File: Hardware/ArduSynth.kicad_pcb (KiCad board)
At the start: 2 copper layers, 71.1 x 45.7 mm, 21 parts, among them J1 STEREO_JACK_3.5MM, J2 STEREO_JACK_3.5MM, P1 ARD_CONN_8, P2 ADR_CONN_6, P3 ARD_CONN_10, P4 ARD_CONN_8, SW1 SW_12X12MM

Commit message: Fixed lables on sch
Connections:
- net N-0000022 renamed /ADJ3
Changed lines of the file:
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@@
     (links 40)
     (no_connects 40)
-    (area 59.400999 86.425309 170.497501 152.806401)
+    (area 93.690999 34.28873 168.560044 81.330001)
     (thickness 1.6)
     (drawings 4)
@@
   (net 1 /ADJ1)
   (net 2 /ADJ2)
-  (net 3 /ADJ4)
-  (net 4 /ADJ5)
-  (net 5 "/AUDIO OUT")
-  (net 6 /CV)
-  (net 7 /TRIGGER)
-  (net 8 N-0000013)
-  (net 9 N-0000018)
-  (net 10 N-0000022)
+  (net 3 /ADJ3)
+  (net 4 /ADJ4)
+  (net 5 /ADJ5)
+  (net 6 "/AUDIO OUT")
+  (net 7 /CV)
+  (net 8 /TRIGGER)
+  (net 9 N-0000014)
+  (net 10 N-0000034)
   (net 11 N-0000035)
   (net 12 N-0000036)
   (net 13 N-0000037)
-  (net 14 N-0000038)
+  (net 14 N-0000039)
   (net 15 VDD)
   (net 16 VSS)
@@
     (add_net /ADJ1)
     (add_net /ADJ2)
+    (add_net /ADJ3)
     (add_net /ADJ4)
     (add_net /ADJ5)
@@
     (add_net /CV)
     (add_net /TRIGGER)
-    (add_net N-0000013)
-    (add_net N-0000018)
-    (add_net N-0000022)
+    (add_net N-0000014)
+    (add_net N-0000034)
     (add_net N-0000035)
     (add_net N-0000036)
     (add_net N-0000037)
-    (add_net N-0000038)
+    (add_net N-0000039)
     (add_net VDD)
     (add_net VSS)
@@
     (pad 1 thru_hole circle (at 3.81 -2.54) (size 1.397 1.397) (drill 0.8128)
       (layers *.Cu *.Mask F.SilkS)
-      (net 7 /TRIGGER)
+      (net 8 /TRIGGER)
     )
     (pad 2 thru_hole circle (at 3.81 2.54) (size 1.397 1.397) (drill 0.8128)
       (layers *.Cu *.Mask F.SilkS)
-      (net 7 /TRIGGER)
+      (net 8 /TRIGGER)
     )
     (pad 1 thru_hole circle (at -3.81 -2.54) (size 1.397 1.397) (drill 0.8128)
       (layers *.Cu *.Mask F.SilkS)
-      (net 7 /TRIGGER)
+      (net 8 /TRIGGER)
     )
     (pad 2 thru_hole circle (at -3.81 2.54) (size 1.397 1.397) (drill 0.8128)
       (layers *.Cu *.Mask F.SilkS)
-      (net 7 /TRIGGER)
+      (net 8 /TRIGGER)
     )
   )
@@
     (pad 1 thru_hole circle (at -5.08 0 180) (size 1.524 1.524) (drill 0.8128)
       (layers *.Cu *.Mask F.SilkS)
-      (net 14 N-0000038)
+      (net 14 N-0000039)
     )
     (pad 2 thru_hole circle (at 5.08 0 180) (size 1.524 1.524) (drill 0.8128)
@@
     (pad 1 thru_hole circle (at -5.08 0) (size 1.524 1.524) (drill 0.8128)
       (layers *.Cu *.Mask F.SilkS)
-      (net 6 /CV)
+      (net 7 /CV)
     )
     (pad 2 thru_hole circle (at 5.08 0) (size 1.524 1.524) (drill 0.8128)
       (layers *.Cu *.Mask F.SilkS)
-      (net 8 N-0000013)
+      (net 9 N-0000014)
     )
     (model discret/resistor.wrl
@@
     (pad 2 thru_hole circle (at 5.08 0 180) (size 1.524 1.524) (drill 0.8128)
       (layers *.Cu *.Mask F.SilkS)
-      (net 14 N-0000038)
+      (net 14 N-0000039)
     )
     (model discret/resistor.wrl
@@
     (pad 1 thru_hole circle (at -1.27 0 180) (size 1.397 1.397) (drill 0.8128)
       (layers *.Cu *.Mask F.SilkS)
-      (net 8 N-0000013)
+      (net 9 N-0000014)
     )
     (pad 2 thru_hole circle (at 1.27 0 180) (size 1.397 1.397) (drill 0.8128)
@@
     (pad 1 thru_hole circle (at -1.27 0) (size 1.397 1.397) (drill 0.8128)
       (layers *.Cu *.Mask F.SilkS)
-      (net 14 N-0000038)
+      (net 14 N-0000039)
     )
     (pad 2 thru_hole circle (at 1.27 0) (size 1.397 1.397) (drill 0.8128)
@@
     (pad 6 thru_hole circle (at 3.81 0) (size 1.397 1.397) (drill 0.8128)
       (layers *.Cu *.Mask F.SilkS)
-      (net 7 /TRIGGER)
+      (net 8 /TRIGGER)
     )
     (pad 7 thru_hole circle (at 6.35 0) (size 1.397 1.397) (drill 0.8128)
@@
     (pad 1 thru_hole rect (at -6.35 0) (size 1.397 1.397) (drill 0.8128)
       (layers *.Cu *.Mask F.SilkS)
-      (net 8 N-0000013)
+      (net 9 N-0000014)
     )
     (pad 2 thru_hole circle (at -3.81 0) (size 1.397 1.397) (drill 0.8128)
       (layers *.Cu *.Mask F.SilkS)
-      (net 4 /ADJ5)
+      (net 5 /ADJ5)
     )
     (pad 3 thru_hole circle (at -1.27 0) (size 1.397 1.397) (drill 0.8128)
       (layers *.Cu *.Mask F.SilkS)
-      (net 3 /ADJ4)
+      (net 4 /ADJ4)
     )
     (pad 4 thru_hole circle (at 1.27 0) (size 1.397 1.397) (drill 0.8128)
       (layers *.Cu *.Mask F.SilkS)
-      (net 10 N-0000022)
+      (net 3 /ADJ3)
     )
     (pad 5 thru_hole circle (at 3.81 0) (size 1.397 1.397) (drill 0.8128)
@@
     (pad 5 thru_hole circle (at -1.27 0) (size 1.397 1.397) (drill 0.8128)
       (layers *.Cu *.Mask F.SilkS)
-      (net 9 N-0000018)
+      (net 10 N-0000034)
     )
     (pad 6 thru_hole circle (at 1.27 0) (size 1.397 1.397) (drill 0.8128)
@@
     (pad 2 thru_hole circle (at 1.27 0 90) (size 1.6764 1.6764) (drill 0.8128)
       (layers *.Cu *.Mask F.SilkS)
-      (net 9 N-0000018)
+      (net 10 N-0000034)
     )
     (model discret/leds/led5_vertical_verde.wrl
@@
     (pad 2 smd rect (at 4.3 -7.05) (size 2.2 2.1)
       (layers F.Cu F.Paste F.Mask)
-      (net 6 /CV)
+      (net 7 /CV)
     )
     (pad 3 smd rect (at 11.7 1.05) (size 2.7 2.1)
       (layers F.Cu F.Paste F.Mask)
-      (net 6 /CV)
+      (net 7 /CV)
     )
     (pad 4 smd rect (at 1.6 -7.05) (size 2 2.1)
@@
     (pad 2 smd rect (at 4.3 -7.05) (size 2.2 2.1)
       (layers F.Cu F.Paste F.Mask)
-      (net 5 "/AUDIO OUT")
+      (net 6 "/AUDIO OUT")
     )
     (pad 3 smd rect (at 11.7 1.05) (size 2.7 2.1)
       (layers F.Cu F.Paste F.Mask)
-      (net 5 "/AUDIO OUT")
+      (net 6 "/AUDIO OUT")
     )
     (pad 4 smd rect (at 1.6 -7.05) (size 2 2.1)
@@
     (pad 2 thru_hole circle (at 5.3 7) (size 1.8 1.8) (drill 1)
       (layers *.Cu *.Mask F.SilkS)
-      (net 3 /ADJ4)
+      (net 4 /ADJ4)
     )
     (pad 3 thru_hole circle (at 7.8 7) (size 1.8 1.8) (drill 1)
@@
     (pad 2 thru_hole circle (at 5.3 7) (size 1.8 1.8) (drill 1)
       (layers *.Cu *.Mask F.SilkS)
-      (net 4 /ADJ5)
+      (net 5 /ADJ5)
     )
     (pad 3 thru_hole circle (at 7.8 7) (size 1.8 1.8) (drill 1)
@@
     (pad 2 thru_hole circle (at 5.3 7) (size 1.8 1.8) (drill 1)
       (layers *.Cu *.Mask F.SilkS)
-      (net 5 "/AUDIO OUT")
+      (net 6 "/AUDIO OUT")
     )
     (pad 3 thru_hole circle (at 7.8 7) (size 1.8 1.8) (drill 1)
@@
     (pad 2 thru_hole circle (at 5.3 7) (size 1.8 1.8) (drill 1)
       (layers *.Cu *.Mask F.SilkS)
-      (net 10 N-0000022)
+      (net 3 /ADJ3)
     )
     (pad 3 thru_hole circle (at 7.8 7) (size 1.8 1.8) (drill 1)

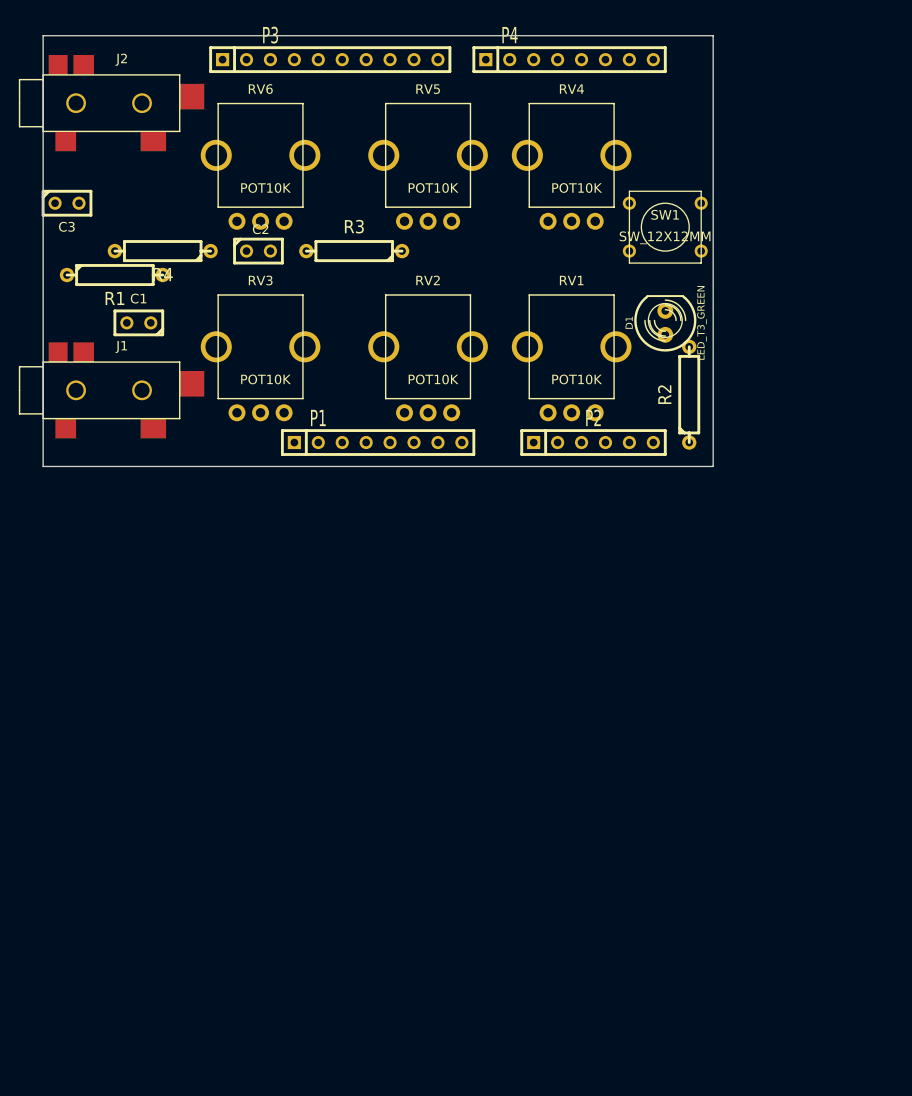
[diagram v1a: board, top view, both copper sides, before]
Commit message: Updated symbols for Arduino and placement
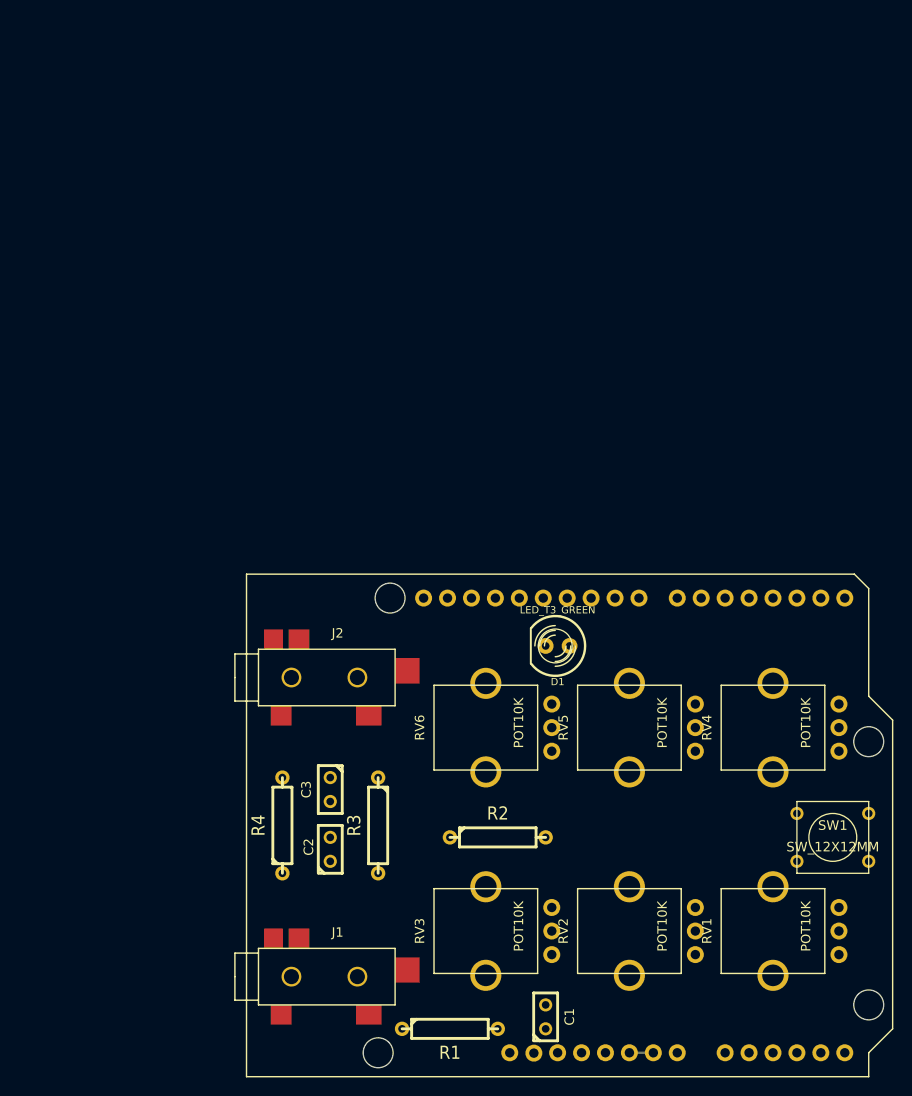
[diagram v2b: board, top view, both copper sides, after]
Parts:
- removed P1, P4: ARD_CONN_8, SIL-8
- removed P2: ADR_CONN_6, SIL-6
- removed P3: ARD_CONN_10, SIL-10
- added U1: ARDUINOR3, ArduinoR3, F.Cu at (118.1, 146.1)
- moved R1 87.6 mm to (139.7, 141.0)
- moved C1 85.4 mm to (149.9, 139.7), turned to 90 degrees
- moved RV3 73.4 mm to (143.5, 135.9), turned to 90 degrees
- moved RV1 72.4 mm to (174.0, 135.9), turned to 90 degrees
- moved RV2 72.4 mm to (158.8, 135.9), turned to 90 degrees
- moved RV6 72.2 mm to (143.5, 114.3), turned to 90 degrees
- moved RV4 71.2 mm to (174.0, 114.3), turned to 90 degrees
- moved RV5 71.2 mm to (158.8, 114.3), turned to 90 degrees
- moved C3 68.2 mm to (127.0, 115.6), turned to 270 degrees
- moved SW1 67.2 mm to (180.3, 120.7)
- moved J1 66.3 mm to (119.4, 138.4)
- moved J2 65.1 mm to (119.4, 106.7)
- moved C2 64.0 mm to (127.0, 121.9), turned to 90 degrees
- moved R4 62.3 mm to (121.9, 119.4), turned to 90 degrees
- moved R3 61.0 mm to (132.1, 119.4), turned to 270 degrees
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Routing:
- net VSS: track 0.00 -> 2.54 mm
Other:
- board outline removed
